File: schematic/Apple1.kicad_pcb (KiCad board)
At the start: 2 copper layers, 167.5 x 124.7 mm, 65 parts, among them J1 RCJ-041, J2 USB_A, J4 PWR, J5 ARM_JTAG_SWD, J6 SLOT, J7 EDGE, J8 12V, J9 -12V, SW1 RST, SW2 CLEAR, SW3 PWR, U1 WD65C02, U10 L7805, U2 6821 (W65C21N), U3 ATSAMD21E18A-A, U4 74LS138, U5 AT28C64B-15PU, U6 AS6C62256, U7 74HC00, U9 LD33CV

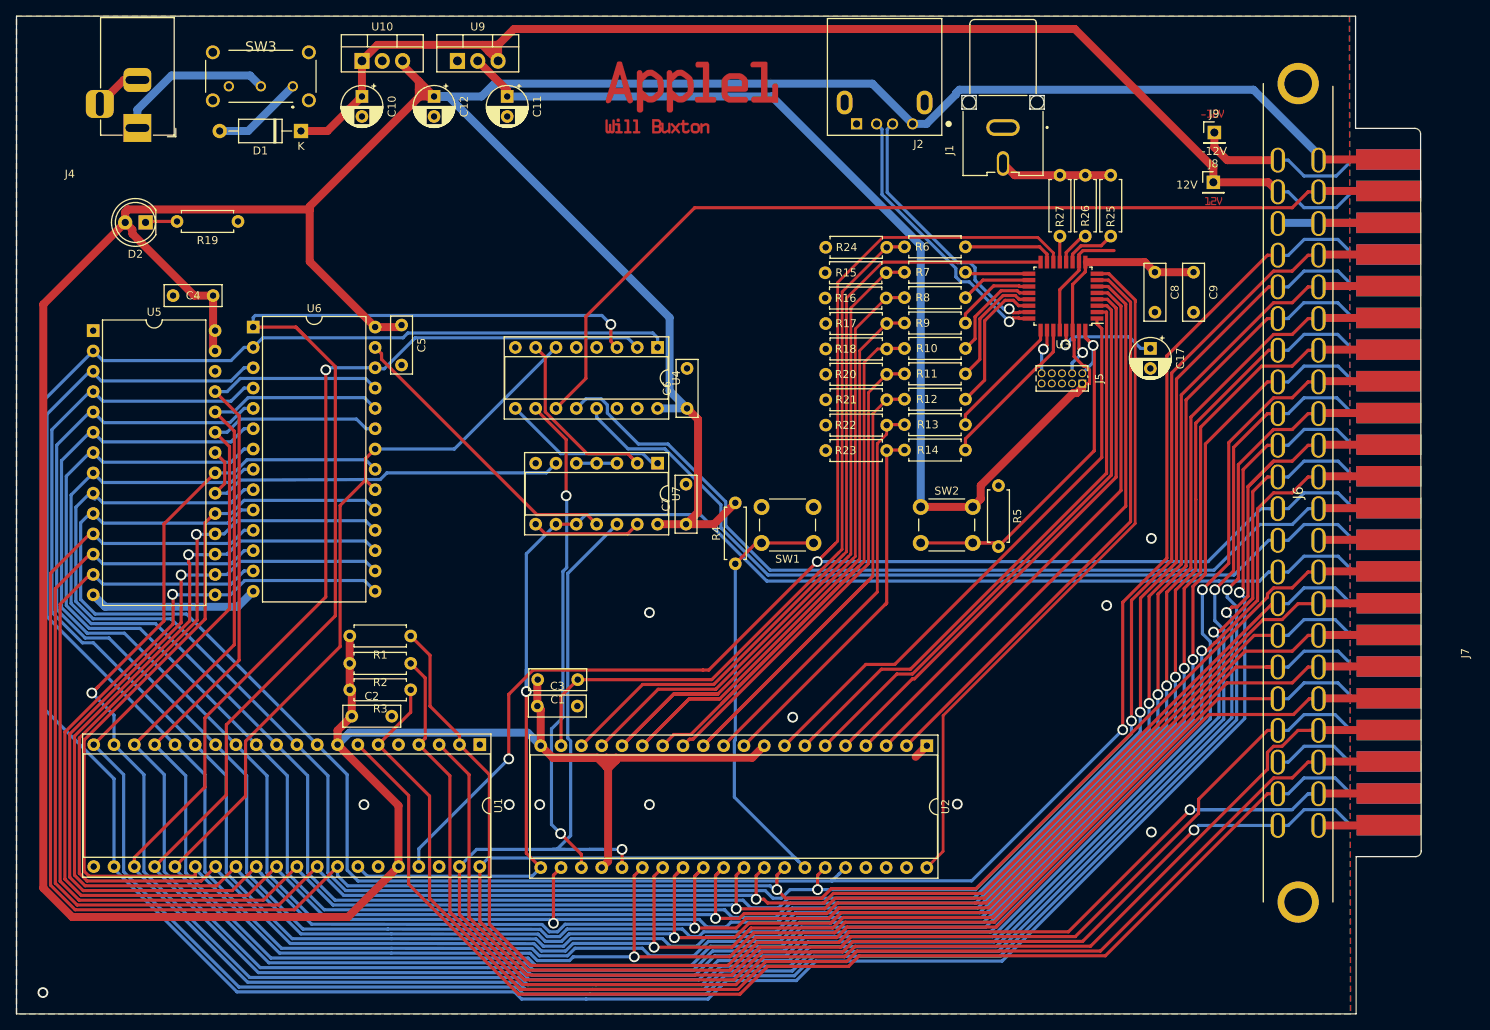
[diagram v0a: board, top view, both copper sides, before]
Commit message: updated pcb with electroplater
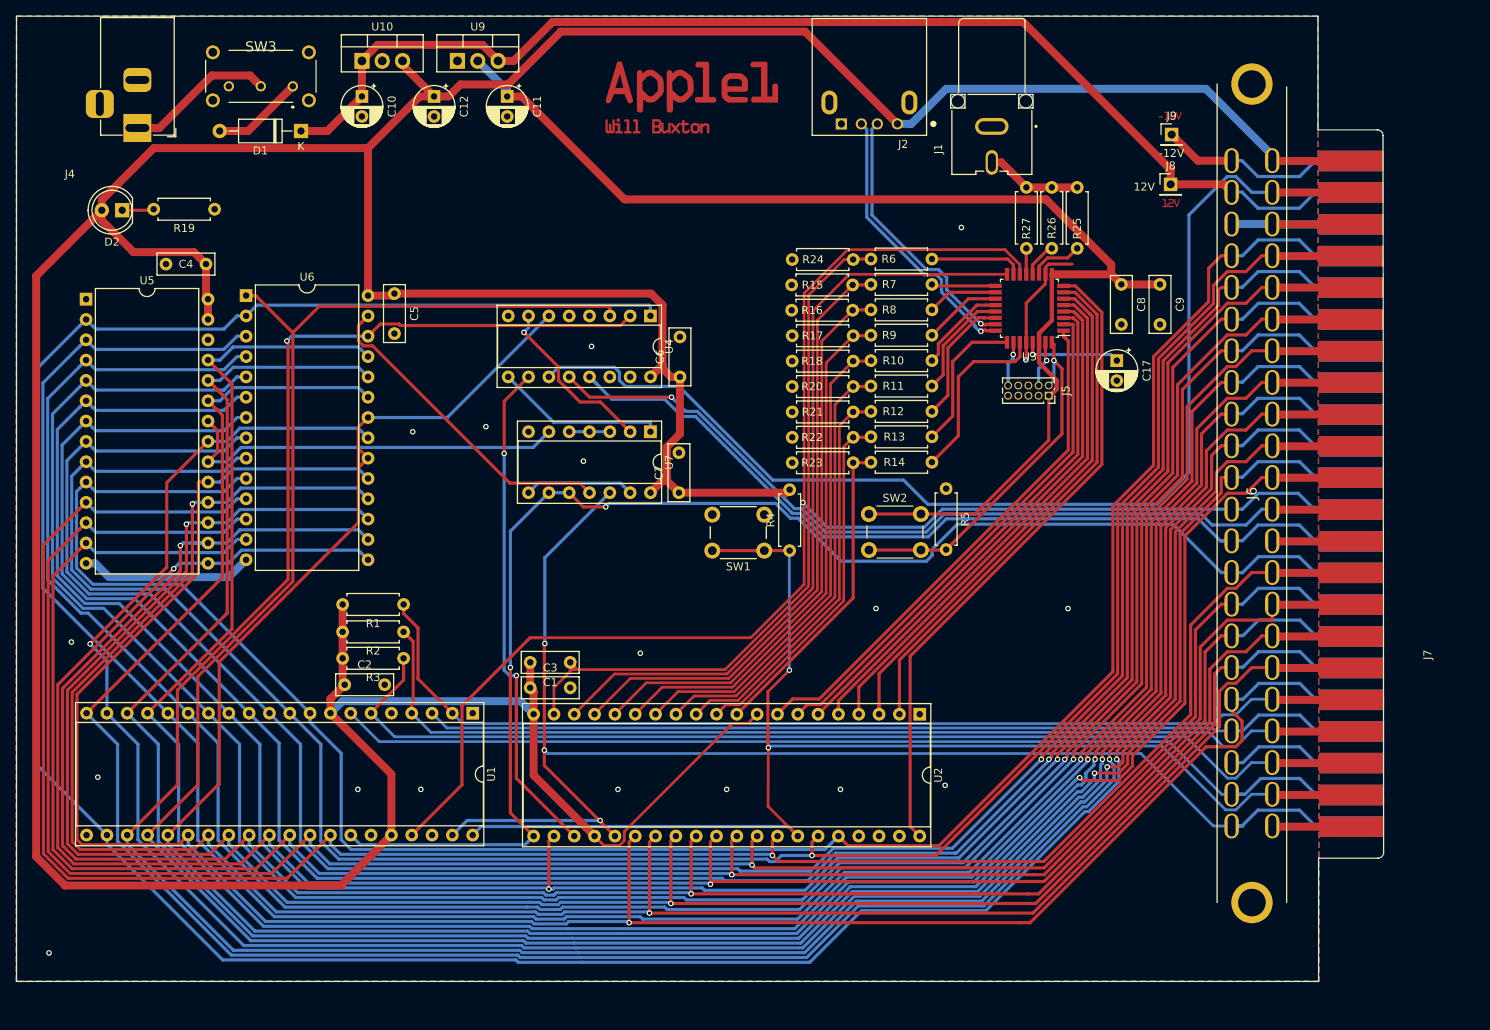
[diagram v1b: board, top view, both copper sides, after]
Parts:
- moved R4 6.99 mm to (128.4, 84.5)
- moved R5 6.55 mm to (148.0, 76.7)
- moved SW2 6.54 mm to (138.3, 79.9)
- moved SW1 6.23 mm to (125.2, 84.5)
- moved J6 5.78 mm to (188.7, 118.9)
- moved G*** 5.34 mm to (176.5, 42.9)
- moved J8 5.34 mm to (176.0, 38.7)
- moved J9 5.34 mm to (176.1, 32.4)
- moved G*** 5.34 mm to (176.0, 32.0)
- moved J7 4.70 mm to (207.6, 97.5)
- moved J5 4.46 mm to (160.8, 65.1)
- moved C17 4.46 mm to (169.3, 60.7)
- moved C8 4.46 mm to (169.9, 51.2)
- moved C9 4.46 mm to (174.7, 51.2)
- moved R10 4.46 mm to (146.2, 60.7)
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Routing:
- net /RESET: track 238.1 -> 166.8 mm, vias 1 -> 2
- net /PHI1O: track 156.4 -> 117.4 mm
- net /IQR: track 170.5 -> 131.9 mm
- net /RDY: track 168.5 -> 130.3 mm
- net /PB2: track 84.2 -> 50.2 mm
- net /NMI: track 166.9 -> 136.4 mm
- net /PHI2O: track 207.0 -> 177.1 mm, vias 2 -> 3
- net /PB4: track 89.6 -> 60.7 mm
- net /SYNC: track 161.1 -> 132.3 mm
- net /$C000: track 119.9 -> 145.1 mm
- net /A14: track 338.6 -> 316.7 mm, vias 2 -> 1
- net /PB6: track 89.8 -> 71.3 mm
- net /PB5: track 82.0 -> 66.0 mm
- net VCC: track 567.8 -> 553.1 mm
- net /A10: track 295.0 -> 284.0 mm
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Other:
- board size 167.5 x 124.7 mm -> 162.8 x 120.7 mm
- net class Default: via_dia 1.35 -> 0.7; via_drill 0.9 -> 0.4
- net class Thic: via_dia 1.35 -> 1; via_drill 0.9 -> 0.6

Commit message: rpi final
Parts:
- removed G***: LOGO, Apple1Title:n12v
- removed G***: LOGO, Apple1Title:12v
- removed G***: LOGO, Title:title
- added C13: 47uF, Capacitor_SMD:C_1206_3216Metric, F.Cu at (158.8, 74.6)
- added C14: 47uF, Capacitor_SMD:C_1206_3216Metric, F.Cu at (178.5, 62.6)
- added C15: 47uF, Capacitor_SMD:C_1206_3216Metric, F.Cu at (164.4, 74.6)
- added C16: 4.7uF, Capacitor_SMD:C_0603_1608Metric_Pad1.08x0.95mm_HandSolder, F.Cu at (172.2, 73.6)
- added C18: 0.1uF, Capacitor_SMD:C_0603_1608Metric_Pad1.08x0.95mm_HandSolder, F.Cu at (195.5, 76.7)
- added C19: 10uF, Capacitor_SMD:C_0603_1608Metric_Pad1.08x0.95mm_HandSolder, F.Cu at (117.5, 64.5)
- added C20: 10uF, Capacitor_SMD:C_0603_1608Metric_Pad1.08x0.95mm_HandSolder, F.Cu at (113.1, 64.5)
- added C21: 0.47uF, Capacitor_SMD:C_0603_1608Metric_Pad1.08x0.95mm_HandSolder, F.Cu at (108.8, 64.5)
- added C22: 0.47uF, Capacitor_SMD:C_0603_1608Metric_Pad1.08x0.95mm_HandSolder, F.Cu at (145.4, 62.9)
- added J3: SLOT, 307-044-520-202:307044520202, F.Cu at (244.5, 128.4)
- added L1: 4.7uH, Inductor_SMD:L_Bourns-SRN4018, F.Cu at (141.6, 61.9)
- added L2: 4.7uH, Inductor_SMD:L_Bourns-SRN4018, F.Cu at (135.5, 61.9)
- added Q1: DMG1012T, Package_TO_SOT_SMD:SOT-523, F.Cu at (171.7, 76.4)
- added Q2: DMG1012T, Package_TO_SOT_SMD:SOT-523, F.Cu at (210.2, 68.4)
- added R28: 2k, Resistor_SMD:R_0603_1608Metric_Pad0.98x0.95mm_HandSolder, F.Cu at (191.2, 76.7)
- added R29: 100k, Resistor_SMD:R_0603_1608Metric, F.Cu at (206.1, 72.6)
- added U11: AP2331W, Package_TO_SOT_SMD:SOT-23, F.Cu at (206.4, 61.5)
- added U12: AP7315DQ-2.5, Package_TO_SOT_SMD:SOT-23-5, F.Cu at (135.6, 50.2)
- added U8: AT28C64B-15PU, Package_DIP:DIP-28_W15.24mm, F.Cu at (137.0, 116.6)
- C1: value 0.01uF -> 0.33uF; footprint Capacitor_THT:C_Rect_L7.0mm_W2.5mm_P5.00mm -> Capacitor_SMD:C_0603_1608Metric_Pad1.08x0.95mm_HandSolder
- C10: value 10uF -> 0.1uF; footprint Capacitor_THT:CP_Radial_D5.0mm_P2.50mm -> Capacitor_THT:C_Rect_L7.0mm_W2.5mm_P5.00mm
- C11: footprint Capacitor_THT:CP_Radial_D5.0mm_P2.50mm -> Capacitor_SMD:C_0603_1608Metric_Pad1.08x0.95mm_HandSolder
- C12: value 1uF -> 10uF; footprint Capacitor_THT:CP_Radial_D5.0mm_P2.50mm -> Capacitor_SMD:C_0603_1608Metric_Pad1.08x0.95mm_HandSolder
- C17: value 1uF -> 0.1uF; footprint Capacitor_THT:CP_Radial_D5.0mm_P2.50mm -> Capacitor_SMD:C_0603_1608Metric_Pad1.08x0.95mm_HandSolder
- C2, C3: footprint Capacitor_THT:C_Rect_L7.0mm_W2.5mm_P5.00mm -> Capacitor_SMD:C_0603_1608Metric_Pad1.08x0.95mm_HandSolder
- C4: value 0.1uF -> 0.01uF
- J1: value RCJ-041 -> PWR; footprint CUI_RCJ-041 -> Connector_BarrelJack:BarrelJack_CUI_PJ-102AH_Horizontal
- J2: value USB_A -> EDGE; footprint UJ2-AH-4-TH:CUI_UJ2-AH-4-TH -> Connector_PCBEdge:EDAC_Edge_307-044-520-202
- J4: value PWR -> 12V; footprint Connector_BarrelJack:BarrelJack_Horizontal -> Connector_PinHeader_2.54mm:PinHeader_1x01_P2.54mm_Vertical
- J5: value ARM_JTAG_SWD -> -12V; footprint Connector_PinSocket_1.27mm:PinSocket_2x05_P1.27mm_Vertical -> Connector_PinHeader_2.54mm:PinHeader_1x01_P2.54mm_Vertical
- J6: value SLOT -> USB_A; footprint 307-044-520-202:307044520202 -> UJ2-AH-4-TH:CUI_UJ2-AH-4-TH
- J7: value EDGE -> RCJ-041; footprint Connector_PCBEdge:EDAC_Edge_307-044-520-202 -> CUI_RCJ-041
- J8: value 12V -> Micro_SD_Card_Det; footprint Connector_PinHeader_2.54mm:PinHeader_1x01_P2.54mm_Vertical -> Connector_Card:microSD_HC_Molex_104031-0811
- J9: value -12V -> HDMI_A; footprint Connector_PinHeader_2.54mm:PinHeader_1x01_P2.54mm_Vertical -> 10029449-111RLF:10029449111RLF
- R10, R11, R12, R13, R14, R6, R7, R8, R9: value 1K -> 2k; footprint Resistor_THT:R_Axial_DIN0207_L6.3mm_D2.5mm_P7.62mm_Horizontal -> Resistor_SMD:R_0603_1608Metric_Pad0.98x0.95mm_HandSolder
- R15, R16, R17, R18, R20, R21, R22, R23, R24: value 2k -> 1K; footprint Resistor_THT:R_Axial_DIN0207_L6.3mm_D2.5mm_P7.62mm_Horizontal -> Resistor_SMD:R_0603_1608Metric_Pad0.98x0.95mm_HandSolder
- R19: value 330 -> 100k; footprint Resistor_THT:R_Axial_DIN0207_L6.3mm_D2.5mm_P7.62mm_Horizontal -> Resistor_SMD:R_0603_1608Metric
- R25: footprint Resistor_THT:R_Axial_DIN0207_L6.3mm_D2.5mm_P7.62mm_Horizontal -> Resistor_SMD:R_0603_1608Metric_Pad0.98x0.95mm_HandSolder
- R26: value 560 -> 100k; footprint Resistor_THT:R_Axial_DIN0207_L6.3mm_D2.5mm_P7.62mm_Horizontal -> Resistor_SMD:R_0603_1608Metric_Pad0.98x0.95mm_HandSolder
- R27: value 220 -> 100k; footprint Resistor_THT:R_Axial_DIN0207_L6.3mm_D2.5mm_P7.62mm_Horizontal -> Resistor_SMD:R_0603_1608Metric_Pad0.98x0.95mm_HandSolder
- R5: value 3.3K -> 330
- SW1: value RST -> PWR; footprint Button_Switch_THT:SW_PUSH_6mm -> EG1224:EG1224
- SW2: value CLEAR -> RST
- SW3: value PWR -> CLEAR; footprint EG1224:EG1224 -> Button_Switch_THT:SW_PUSH_6mm
- U1: value WD65C02 -> 74LS138; footprint Package_DIP:DIP-40_W15.24mm_Socket -> Package_DIP:DIP-16_W7.62mm_Socket
- U10: value L7805 -> ESD5384; footprint Package_TO_SOT_THT:TO-220-3_Vertical -> SW-On-Semi:WLCSP9-1.14x1.14mm
- U2: value 6821 (W65C21N) -> AS6C62256; footprint Package_DIP:DIP-40_W15.24mm_Socket -> Package_DIP:DIP-28_W15.24mm
- U3: value ATSAMD21E18A-A -> WD65C02; footprint Package_QFP:TQFP-32_7x7mm_P0.8mm -> Package_DIP:DIP-40_W15.24mm_Socket
- U4: value 74LS138 -> 74HC00; footprint Package_DIP:DIP-16_W7.62mm_Socket -> Package_DIP:DIP-14_W7.62mm_Socket
- U5: value AT28C64B-15PU -> PAM2306AYPKE; footprint Package_DIP:DIP-28_W15.24mm -> Package_DFN_QFN:WDFN-12-1EP_3x3mm_P0.45mm_EP1.7x2.5mm
- U6: value AS6C62256 -> 6821 (W65C21N); footprint Package_DIP:DIP-28_W15.24mm -> Package_DIP:DIP-40_W15.24mm_Socket
- U7: value 74HC00 -> L7805; footprint Package_DIP:DIP-14_W7.62mm_Socket -> Package_TO_SOT_THT:TO-220-3_Vertical
- U9: value LD33CV -> RaspberryPi-CM3+L; footprint Package_TO_SOT_THT:TO-220-3_Vertical -> 1717254-4:17172544
- moved SW3 151.3 mm to (207.3, 81.4), turned to 0 degrees
- moved J2 143.0 mm to (263.1, 106.9), turned to 90 degrees
- moved U6 131.9 mm to (175.9, 116.5), turned to 90 degrees
- moved U10 112.7 mm to (177.1, 70.7)
- moved U5 107.1 mm to (147.3, 61.4)
- moved U9 106.7 mm to (189.9, 51.1)
- moved R19 95.4 mm to (149.6, 62.9), turned to 0 degrees
- moved D2 94.5 mm to (125.1, 91.9), turned to 0 degrees
- moved J4 94.2 mm to (136.3, 61.4), turned to 0 degrees
- moved C2 87.2 mm to (149.8, 60.3)
- moved U3 85.7 mm to (175.8, 138.0), turned to 90 degrees
- moved R15 82.6 mm to (210.8, 60.5)
- moved SW2 80.8 mm to (219.1, 81.0)
- moved C10 80.1 mm to (143.3, 69.4), turned to 0 degrees
- moved J6 80.1 mm to (166.2, 42.0), turned to 180 degrees
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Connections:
- C1 pad 1: /CB2 -> +12V
- C1 pad 2: VCC -> GND
- C10 pad 1: +12V -> +5V
- C11 pad 1: +3V3 -> +5V
- C12 pad 1: VCC -> +5V
- C17 pad 1: Net-(C17-Pad1) -> +5V
- C2 pad 1: VCC -> GND
- C2 pad 2: GND -> Net-(C2-Pad2)
- C3 pad 1: VCC -> +5V
- C4 pad 1: VCC -> /CB2
- C4 pad 2: GND -> +5V
- C5 pad 1: VCC -> +5V
- C6 pad 1: VCC -> +5V
- C7 pad 1: VCC -> +5V
- C8 pad 1: +3V3 -> +5V
- C9 pad 1: +3V3 -> +5V
- D2 pad 2: VCC -> +5V
- J1 pad 1: GND -> Net-(J1-Pad1)
- J1 pad 2: Net-(J1-Pad2) -> GND
- J2 pad 1: VCC -> /RF
- J2 pad 2: /KEYD- -> /PHI2O
- J2 pad 3: /KEYD+ -> /RESET
- J2 pad 4: GND -> /SYNC
- J2 pad 5: GND -> /NMI
- J4 pad 1: Net-(J4-Pad1) -> +12V
- J5 pad 1: +3V3 -> -12V
- J6 pad 1: /RF -> +5V
- J6 pad 2: /PHI2O -> /RaspberryPi/USB_D-
- J6 pad 3: /RESET -> /RaspberryPi/USB_D+
- J6 pad 4: /SYNC -> GND
- J6 pad 5: /NMI -> GND
- J7 pad 1: /RF -> GND
- J7 pad 2: /PHI2O -> /RaspberryPi/TVDAC
- J8 pad 1: +12V -> /RaspberryPi/SDX_D2
- J9 pad 1: -12V -> /RaspberryPi/HDMI_D2_P
- R1 pad 2: VCC -> +5V
- R10 pad 1: Net-(R10-Pad1) -> GND
- R11 pad 1: Net-(R11-Pad1) -> GND
- R11 pad 2: /PB3 -> /PB5
- R12 pad 1: Net-(R12-Pad1) -> GND
- R12 pad 2: /PB2 -> /PB6
- R13 pad 1: Net-(R13-Pad1) -> GND
- R13 pad 2: /PB1 -> /DA
- R14 pad 1: Net-(R14-Pad1) -> GND
- R14 pad 2: /PB0 -> /CB2
- R15 pad 1: GND -> Net-(R15-Pad1)
- R15 pad 2: /DA -> /RESET
- R16 pad 1: GND -> Net-(R16-Pad1)
- R16 pad 2: /PB6 -> /PB0
- R17 pad 1: GND -> Net-(R17-Pad1)
- R17 pad 2: /PB5 -> /PB1
- R18 pad 1: GND -> Net-(R18-Pad1)
- R18 pad 2: /PB4 -> /PB2
- R19 pad 1: GND -> +5V
- R19 pad 2: Net-(D2-Pad1) -> Net-(C2-Pad2)
- R2 pad 2: VCC -> +5V
- R20 pad 1: GND -> Net-(R20-Pad1)
- R21 pad 1: GND -> Net-(R21-Pad1)
- R21 pad 2: /PB2 -> /PB4
- R22 pad 1: GND -> Net-(R22-Pad1)
- R22 pad 2: /PB1 -> /PB5
- R23 pad 1: GND -> Net-(R23-Pad1)
- R23 pad 2: /PB0 -> /PB6
- R24 pad 1: GND -> Net-(R24-Pad1)
- R24 pad 2: /CB2 -> /DA
- R25 pad 2: Net-(J1-Pad2) -> /CB2
- R26 pad 1: Net-(R26-Pad1) -> /STROBE
- R26 pad 2: Net-(J1-Pad2) -> GND
- R27 pad 1: Net-(R27-Pad1) -> /PA0
- R27 pad 2: Net-(J1-Pad2) -> GND
- R3 pad 2: VCC -> +5V
- R4 pad 2: VCC -> +5V
- R5 pad 2: /SWDIO -> Net-(D2-Pad1)
- R6 pad 1: Net-(R6-Pad1) -> GND
- R6 pad 2: /CB2 -> /PB0
- R7 pad 1: Net-(R7-Pad1) -> GND
- R7 pad 2: /DA -> /PB1
- R8 pad 1: Net-(R8-Pad1) -> GND
- R8 pad 2: /PB6 -> /PB2
- R9 pad 1: Net-(R9-Pad1) -> GND
- R9 pad 2: /PB5 -> /PB3
- SW1 pad 1: /RESET -> Net-(D1-Pad2)
- SW1 pad 2: GND -> Net-(J1-Pad1)
- SW2 pad 1: +3V3 -> /RESET
- SW2 pad 2: /SWDIO -> GND
- SW3 pad 1: Net-(D1-Pad2) -> GND
- SW3 pad 2: Net-(J4-Pad1) -> /RaspberryPi/CLEAR
- U1 pad 1: (no net) -> /A12
- U1 pad 10: /A1 -> /$D000
- U1 pad 11: /A2 -> /$C000
- U1 pad 12: /A3 -> /$B000
- U1 pad 13: /A4 -> /$A000
- U1 pad 14: /A5 -> (no net)
- U1 pad 15: /A6 -> (no net)
- U1 pad 16: /A7 -> +5V
- U1 pad 2: /RDY -> /A13
- U1 pad 3: /PHI1O -> /A14
- U1 pad 4: /IQR -> GND
- U1 pad 5: (no net) -> GND
- U1 pad 6: /NMI -> /A15
- U1 pad 7: /SYNC -> /$F000
- U1 pad 8: VCC -> GND
- U1 pad 9: /A0 -> /$E000
- U2 pad 1: GND -> /A14
- U2 pad 10: /PB0 -> /A0
- U2 pad 11: /PB1 -> /D0
- U2 pad 12: /PB2 -> /D1
- U2 pad 13: /PB3 -> /D2
- U2 pad 14: /PB4 -> GND
- U2 pad 15: /PB5 -> /D3
- U2 pad 16: /PB6 -> /D4
- U2 pad 17: /DA -> /D5
- U2 pad 18: /RDA -> /D6
- U2 pad 19: /CB2 -> /D7
- U2 pad 2: /PA0 -> /A12
- U2 pad 20: VCC -> /A15
- U2 pad 21: /RW -> /A10
- U2 pad 22: /A4 -> /A15
- U2 pad 23: /$D000 -> /A11
- U2 pad 24: VCC -> /A9
- U2 pad 25: /PHI2O -> /A8
- U2 pad 26: /D7 -> /A13
- U2 pad 27: /D6 -> /WE
- U2 pad 28: /D5 -> +5V
- U2 pad 3: /PA1 -> /A7
- U2 pad 4: /PA2 -> /A6
- U2 pad 5: /PA3 -> /A5
- U2 pad 6: /PA4 -> /A4
- U2 pad 7: /PA5 -> /A3
- U2 pad 8: /PA6 -> /A2
- U2 pad 9: VCC -> /A1
- U3 pad 1: /PA6 -> (no net)
- U3 pad 10: GND -> /A1
- U3 pad 11: Net-(R25-Pad1) -> /A2
- U3 pad 12: Net-(R26-Pad1) -> /A3
- U3 pad 13: Net-(R27-Pad1) -> /A4
- U3 pad 14: /PHI2 -> /A5
- U3 pad 15: Net-(R6-Pad1) -> /A6
- U3 pad 16: /RDA -> /A7
- U3 pad 17: Net-(R7-Pad1) -> /A8
- U3 pad 18: Net-(R8-Pad1) -> /A9
- U3 pad 19: Net-(R9-Pad1) -> /A10
- U3 pad 2: /PA5 -> /RDY
- U3 pad 20: Net-(R10-Pad1) -> /A11
- U3 pad 21: Net-(R11-Pad1) -> GND
- U3 pad 22: Net-(R12-Pad1) -> /A12
- U3 pad 23: /KEYD- -> /A13
- U3 pad 24: /KEYD+ -> /A14
- U3 pad 25: Net-(R13-Pad1) -> /A15
- U3 pad 26: /RST -> /D7
- U3 pad 27: Net-(R14-Pad1) -> /D6
- U3 pad 28: GND -> /D5
- U3 pad 29: Net-(C17-Pad1) -> /D4
- U3 pad 3: /PA4 -> /PHI1O
- U3 pad 30: +3V3 -> /D3
- U3 pad 31: /SWCLK -> /D2
- U3 pad 32: /SWDIO -> /D1
- U3 pad 4: /PA3 -> /IQR
- U3 pad 5: /PA2 -> (no net)
- U3 pad 6: /PA1 -> /NMI
- U3 pad 7: /PA0 -> /SYNC
- U3 pad 8: /STROBE -> +5V
- U3 pad 9: +3V3 -> /A0
- U4 pad 1: /A12 -> /$E000
- U4 pad 10: /$D000 -> /RW
- U4 pad 11: /$C000 -> /WE
- U4 pad 12: /$B000 -> /PHI2O
- U4 pad 13: /$A000 -> Net-(U4-Pad13)
- U4 pad 14: (no net) -> +5V
- U4 pad 2: /A13 -> /$F000
- U4 pad 3: /A14 -> Net-(U4-Pad3)
- U4 pad 4: GND -> Net-(U4-Pad3)
- U4 pad 5: GND -> Net-(U4-Pad3)
- U4 pad 6: /A15 -> Net-(U4-Pad6)
- U4 pad 7: /$F000 -> GND
- U4 pad 8: GND -> Net-(U4-Pad13)
- U4 pad 9: /$E000 -> /RW
- U5 pad 1: (no net) -> +5V
- U5 pad 10: /A0 -> +1V8
- U5 pad 11: /D0 -> (no net)
- U5 pad 12: /D1 -> Net-(C2-Pad2)
- U5 pad 13: /D2 -> GND
- U5 pad 2: /A12 -> Net-(L2-Pad1)
- U5 pad 3: /A7 -> GND
- U5 pad 4: /A6 -> +3V3
- U5 pad 5: /A5 -> (no net)
- U5 pad 6: /A4 -> +5V
- U5 pad 7: /A3 -> +5V
- U5 pad 8: /A2 -> Net-(L1-Pad1)
- U5 pad 9: /A1 -> GND
- U6 pad 1: /A14 -> GND
- U6 pad 10: /A0 -> /PB0
- U6 pad 11: /D0 -> /PB1
- U6 pad 12: /D1 -> /PB2
- U6 pad 13: /D2 -> /PB3
- U6 pad 14: GND -> /PB4
- U6 pad 15: /D3 -> /PB5
- U6 pad 16: /D4 -> /PB6
- U6 pad 17: /D5 -> /DA
- U6 pad 18: /D6 -> /RDA
- U6 pad 19: /D7 -> /CB2
- U6 pad 2: /A12 -> /PA0
- U6 pad 20: /A15 -> +5V
- U6 pad 21: /A10 -> /RW
- U6 pad 22: /A15 -> /A4
- U6 pad 23: /A11 -> /$D000
- U6 pad 24: /A9 -> +5V
- U6 pad 25: /A8 -> /PHI2O
- U6 pad 26: /A13 -> /D7
- U6 pad 27: /WE -> /D6
- U6 pad 28: VCC -> /D5
- U6 pad 3: /A7 -> /PA1
- U6 pad 4: /A6 -> /PA2
- U6 pad 5: /A5 -> /PA3
- U6 pad 6: /A4 -> /PA4
- U6 pad 7: /A3 -> /PA5
- U6 pad 8: /A2 -> /PA6
- U6 pad 9: /A1 -> +5V
- U7 pad 1: /$E000 -> +12V
- U7 pad 2: /$F000 -> GND
- U7 pad 3: Net-(U7-Pad3) -> +5V
- U9 pad 2: +3V3 -> (no net)
- U9 pad 3: +12V -> Net-(R15-Pad1)
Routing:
- net VCC: track 553.1 -> 0.00 mm
- net /A12: track 352.5 -> 0.00 mm, vias 1 -> 0
- net /A14: track 316.7 -> 0.00 mm, vias 1 -> 0
- net /A13: track 315.8 -> 0.00 mm, vias 2 -> 0
- net /A11: track 292.3 -> 0.00 mm, vias 1 -> 0
- net /A7: track 290.1 -> 0.00 mm, vias 1 -> 0
- net /A9: track 289.3 -> 0.00 mm, vias 1 -> 0
- net /A4: track 288.2 -> 0.00 mm, vias 2 -> 0
- net /A8: track 287.7 -> 0.00 mm, vias 1 -> 0
- net /A6: track 287.7 -> 0.00 mm, vias 1 -> 0
- net /A15: track 287.2 -> 0.00 mm, vias 1 -> 0
- net /A10: track 284.0 -> 0.00 mm, vias 2 -> 0
- net /A5: track 283.3 -> 0.00 mm, vias 1 -> 0
- net /A3: track 276.8 -> 0.00 mm, vias 1 -> 0
- net /A2: track 274.9 -> 0.00 mm, vias 1 -> 0
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- removed copper zone on B.Cu, net GND
- removed copper zone on F.Cu, net GND
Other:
- board size 162.8 x 120.7 mm -> 8.2 x 91 mm
- copper layers 2 -> 4
- net class HDMI_dPair added: clearance 0.2, trace_width 0.2, via_dia 0.5, via_drill 0.2
- net class PWR added: clearance 0.2, trace_width 1, via_dia 1, via_drill 0.6
- net class Thic removed
- net class USB_dPair added: clearance 0.2, trace_width 0.2, via_dia 1, via_drill 0.6
- rule trace_min: 0.2 -> 0.1
- rule via_min_drill: 0.3 -> 0.127
- rule via_min_size: 0.4 -> 0.3

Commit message: completed schematic
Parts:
- removed R12, R13, R14, R28: 2k, Resistor_SMD:R_0603_1608Metric_Pad0.98x0.95mm_HandSolder
- removed R15, R16, R17, R18, R20, R21, R22, R23, R24, R25: 1K, Resistor_SMD:R_0603_1608Metric_Pad0.98x0.95mm_HandSolder
- removed R19, R29: 100k, Resistor_SMD:R_0603_1608Metric
- removed R26, R27: 100k, Resistor_SMD:R_0603_1608Metric_Pad0.98x0.95mm_HandSolder
- added U13: TXB0104D, Package_SO:SOIC-14_3.9x8.7mm_P1.27mm, F.Cu at (193.0, 68.7)
- added U14: TXB0104D, Package_SO:SOIC-14_3.9x8.7mm_P1.27mm, F.Cu at (224.7, 68.7)
- added U15: TXB0104D, Package_SO:SOIC-14_3.9x8.7mm_P1.27mm, F.Cu at (203.6, 68.7)
- added U16: ESD5384, SW-On-Semi:WLCSP9-1.14x1.14mm, F.Cu at (201.5, 34.0)
- added U17: AP2331W, Package_TO_SOT_SMD:SOT-23, F.Cu at (208.5, 34.5)
- C10: value 0.1uF -> 0.01uF
- C11, C12: value 10uF -> 0.1uF; footprint Capacitor_SMD:C_0603_1608Metric_Pad1.08x0.95mm_HandSolder -> Capacitor_THT:C_Rect_L7.0mm_W2.5mm_P5.00mm
- C13, C14, C15: value 47uF -> 0.1uF; footprint Capacitor_SMD:C_1206_3216Metric -> Capacitor_THT:C_Rect_L7.0mm_W2.5mm_P5.00mm
- C16: value 4.7uF -> 0.1uF; footprint Capacitor_SMD:C_0603_1608Metric_Pad1.08x0.95mm_HandSolder -> Capacitor_THT:C_Rect_L7.0mm_W2.5mm_P5.00mm
- C17, C18: value 0.1uF -> 47uF; footprint Capacitor_SMD:C_0603_1608Metric_Pad1.08x0.95mm_HandSolder -> Capacitor_SMD:C_1206_3216Metric
- C19: value 10uF -> 47uF; footprint Capacitor_SMD:C_0603_1608Metric_Pad1.08x0.95mm_HandSolder -> Capacitor_SMD:C_1206_3216Metric
- C20: value 10uF -> 4.7uF
- C21, C22: value 0.47uF -> 0.1uF
- C4: value 0.01uF -> 10uF; footprint Capacitor_THT:C_Rect_L7.0mm_W2.5mm_P5.00mm -> Capacitor_SMD:C_0603_1608Metric_Pad1.08x0.95mm_HandSolder
- C5, C6, C7: value 0.1uF -> 10uF; footprint Capacitor_THT:C_Rect_L7.0mm_W2.5mm_P5.00mm -> Capacitor_SMD:C_0603_1608Metric_Pad1.08x0.95mm_HandSolder
- C8, C9: value 0.1uF -> 0.47uF; footprint Capacitor_THT:C_Rect_L7.0mm_W2.5mm_P5.00mm -> Capacitor_SMD:C_0603_1608Metric_Pad1.08x0.95mm_HandSolder
- J6: value USB_A -> Micro_SD_Card_Det; footprint UJ2-AH-4-TH:CUI_UJ2-AH-4-TH -> Connector_Card:microSD_HC_Molex_104031-0811
- J8: value Micro_SD_Card_Det -> USB_A; footprint Connector_Card:microSD_HC_Molex_104031-0811 -> UJ2-AH-4-TH:CUI_UJ2-AH-4-TH
- R10, R11, R7, R8, R9: value 2k -> 100k; footprint Resistor_SMD:R_0603_1608Metric_Pad0.98x0.95mm_HandSolder -> Resistor_SMD:R_0603_1608Metric
- R4: value 3.3k -> 100k; footprint Resistor_THT:R_Axial_DIN0207_L6.3mm_D2.5mm_P7.62mm_Horizontal -> Resistor_SMD:R_0603_1608Metric
- R5: value 330 -> 3.3k
- R6: value 2k -> 330; footprint Resistor_SMD:R_0603_1608Metric_Pad0.98x0.95mm_HandSolder -> Resistor_THT:R_Axial_DIN0207_L6.3mm_D2.5mm_P7.62mm_Horizontal
- U1: value 74LS138 -> WD65C02; footprint Package_DIP:DIP-16_W7.62mm_Socket -> Package_DIP:DIP-40_W15.24mm_Socket
- U10: value ESD5384 -> AP7315DQ-2.5; footprint SW-On-Semi:WLCSP9-1.14x1.14mm -> Package_TO_SOT_SMD:SOT-23-5
- U11: value AP2331W -> TXB0104D; footprint Package_TO_SOT_SMD:SOT-23 -> Package_SO:SOIC-14_3.9x8.7mm_P1.27mm
- U12: value AP7315DQ-2.5 -> TXB0104D; footprint Package_TO_SOT_SMD:SOT-23-5 -> Package_SO:SOIC-14_3.9x8.7mm_P1.27mm
- U2: value AS6C62256 -> 6821 (W65C21N); footprint Package_DIP:DIP-28_W15.24mm -> Package_DIP:DIP-40_W15.24mm_Socket
- U3: value WD65C02 -> AS6C62256; footprint Package_DIP:DIP-40_W15.24mm_Socket -> Package_DIP:DIP-28_W15.24mm
- U4: value 74HC00 -> AT28C64B-15PU; footprint Package_DIP:DIP-14_W7.62mm_Socket -> Package_DIP:DIP-28_W15.24mm
- U5: value PAM2306AYPKE -> 74LS138; footprint Package_DFN_QFN:WDFN-12-1EP_3x3mm_P0.45mm_EP1.7x2.5mm -> Package_DIP:DIP-16_W7.62mm_Socket
- U6: value 6821 (W65C21N) -> RaspberryPi-CM3+L; footprint Package_DIP:DIP-40_W15.24mm_Socket -> 1717254-4:17172544
- U8: value AT28C64B-15PU -> PAM2306AYPKE; footprint Package_DIP:DIP-28_W15.24mm -> Package_DFN_QFN:WDFN-12-1EP_3x3mm_P0.45mm_EP1.7x2.5mm
- U9: value RaspberryPi-CM3+L -> 74HC00; footprint 1717254-4:17172544 -> Package_DIP:DIP-14_W7.62mm_Socket
- moved C20 116.4 mm to (221.5, 22.2), turned to 270 degrees
- moved J4 112.1 mm to (244.5, 32.0)
- moved J5 112.1 mm to (249.1, 32.0)
- moved C21 106.7 mm to (211.2, 34.4), turned to 90 degrees
- moved U3 83.4 mm to (115.7, 80.1), turned to 0 degrees
- moved U12 80.8 mm to (214.2, 68.7), turned to 270 degrees
- moved U2 80.5 mm to (217.0, 128.4), turned to 270 degrees
- moved R1 79.0 mm to (161.4, 125.0), turned to 90 degrees
- moved U6 78.7 mm to (202.9, 42.5), turned to 0 degrees
- moved R2 73.0 mm to (156.3, 125.0), turned to 90 degrees
- moved R5 72.5 mm to (179.7, 69.0), turned to 270 degrees
- moved U8 71.1 mm to (153.2, 47.3), turned to 0 degrees
- moved R3 70.0 mm to (151.3, 125.0), turned to 90 degrees
- moved C22 66.9 mm to (205.9, 34.4), turned to 270 degrees
- moved J6 66.2 mm to (230.6, 26.6), turned to 270 degrees
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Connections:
- C10 pad 1: +5V -> /CB2
- C10 pad 2: GND -> +5V
- C13 pad 1: +1V8 -> +5V
- C14 pad 1: +3V3 -> +5V
- C16 pad 1: +3V3 -> +5V
- C17 pad 1: +5V -> +1V8
- C18 pad 1: +5VA -> +3V3
- C19 pad 1: +1V8 -> +5V
- C2 pad 1: GND -> +5V
- C2 pad 2: Net-(C2-Pad2) -> GND
- C21 pad 1: +3V3 -> +5V
- C22 pad 1: +2V5 -> +5VA
- C3 pad 1: +5V -> GND
- C3 pad 2: GND -> Net-(C3-Pad2)
- C4 pad 1: /CB2 -> +5V
- C4 pad 2: +5V -> GND
- C6 pad 1: +5V -> +1V8
- C7 pad 1: +5V -> +3V3
- C8 pad 1: +5V -> +3V3
- C9 pad 1: +5V -> +2V5
- J6 pad 1: +5V -> /RaspberryPi/SDX_D2
- J6 pad 2: /RaspberryPi/USB_D- -> /RaspberryPi/SDX_D3
- J6 pad 3: /RaspberryPi/USB_D+ -> /RaspberryPi/SDX_CMD
- J6 pad 4: GND -> +3V3
- J6 pad 5: GND -> /RaspberryPi/SDX_CLK
- J8 pad 1: /RaspberryPi/SDX_D2 -> +5V
- J8 pad 2: /RaspberryPi/SDX_D3 -> /RaspberryPi/USB_D-
- J8 pad 3: /RaspberryPi/SDX_CMD -> /RaspberryPi/USB_D+
- J8 pad 4: +3V3 -> GND
- J8 pad 5: /RaspberryPi/SDX_CLK -> GND
- R10 pad 1: GND -> /RaspberryPi/RP_DA
- R10 pad 2: /PB4 -> GND
- R11 pad 1: GND -> /RaspberryPi/HDMI_HPD_N
- R11 pad 2: /PB5 -> +1V8
- R4 pad 1: /RESET -> +5V
- R4 pad 2: +5V -> Net-(C3-Pad2)
- R5 pad 1: GND -> /RESET
- R5 pad 2: Net-(D2-Pad1) -> +5V
- R6 pad 2: /PB0 -> Net-(D2-Pad1)
- R7 pad 1: GND -> /RaspberryPi/RP_STB
- R7 pad 2: /PB1 -> GND
- R8 pad 1: GND -> /RaspberryPi/RP_PB6
- R8 pad 2: /PB2 -> GND
- R9 pad 1: GND -> /RaspberryPi/RP_PA0
- R9 pad 2: /PB3 -> GND
- U1 pad 1: /A12 -> (no net)
- U1 pad 10: /$D000 -> /A1
- U1 pad 11: /$C000 -> /A2
- U1 pad 12: /$B000 -> /A3
- U1 pad 13: /$A000 -> /A4
- U1 pad 14: (no net) -> /A5
- U1 pad 15: (no net) -> /A6
- U1 pad 16: +5V -> /A7
- U1 pad 2: /A13 -> /RDY
- U1 pad 3: /A14 -> /PHI1O
- U1 pad 4: GND -> /IQR
- U1 pad 5: GND -> (no net)
- U1 pad 6: /A15 -> /NMI
- U1 pad 7: /$F000 -> /SYNC
- U1 pad 8: GND -> +5V
- U1 pad 9: /$E000 -> /A0
- U11 pad 1: GND -> +3V3
- U11 pad 2: +5VA -> /RaspberryPi/RP_STB
- U11 pad 3: +5V -> /RaspberryPi/RP_PA0
- U12 pad 2: GND -> /RaspberryPi/RP_PB0
- U12 pad 3: +3V3 -> /RaspberryPi/RP_PB1
- U12 pad 4: (no net) -> /RaspberryPi/RP_PB2
- U12 pad 5: +2V5 -> /RaspberryPi/RP_PB3
- U2 pad 1: /A14 -> GND
- U2 pad 10: /A0 -> /PB0
- U2 pad 11: /D0 -> /PB1
- U2 pad 12: /D1 -> /PB2
- U2 pad 13: /D2 -> /PB3
- U2 pad 14: GND -> /PB4
- U2 pad 15: /D3 -> /PB5
- U2 pad 16: /D4 -> /PB6
- U2 pad 17: /D5 -> /DA
- U2 pad 18: /D6 -> /RDA
- U2 pad 19: /D7 -> /CB2
- U2 pad 2: /A12 -> /PA0
- U2 pad 20: /A15 -> +5V
- U2 pad 21: /A10 -> /RW
- U2 pad 22: /A15 -> /A4
- U2 pad 23: /A11 -> /$D000
- U2 pad 24: /A9 -> +5V
- U2 pad 25: /A8 -> /PHI2O
- U2 pad 26: /A13 -> /D7
- U2 pad 27: /WE -> /D6
- U2 pad 28: +5V -> /D5
- U2 pad 3: /A7 -> /PA1
- U2 pad 4: /A6 -> /PA2
- U2 pad 5: /A5 -> /PA3
- U2 pad 6: /A4 -> /PA4
- U2 pad 7: /A3 -> /PA5
- U2 pad 8: /A2 -> /PA6
- U2 pad 9: /A1 -> +5V
- U3 pad 1: (no net) -> /A14
- U3 pad 10: /A1 -> /A0
- U3 pad 11: /A2 -> /D0
- U3 pad 12: /A3 -> /D1
- U3 pad 13: /A4 -> /D2
- U3 pad 14: /A5 -> GND
- U3 pad 15: /A6 -> /D3
- U3 pad 16: /A7 -> /D4
- U3 pad 17: /A8 -> /D5
- U3 pad 18: /A9 -> /D6
- U3 pad 19: /A10 -> /D7
- U3 pad 2: /RDY -> /A12
- U3 pad 20: /A11 -> /A15
- U3 pad 21: GND -> /A10
- U3 pad 22: /A12 -> /A15
- U3 pad 23: /A13 -> /A11
- U3 pad 24: /A14 -> /A9
- U3 pad 25: /A15 -> /A8
- U3 pad 26: /D7 -> /A13
- U3 pad 27: /D6 -> /WE
- U3 pad 28: /D5 -> +5V
- U3 pad 3: /PHI1O -> /A7
- U3 pad 4: /IQR -> /A6
- U3 pad 5: (no net) -> /A5
- U3 pad 6: /NMI -> /A4
- U3 pad 7: /SYNC -> /A3
- U3 pad 8: +5V -> /A2
- U3 pad 9: /A0 -> /A1
- U4 pad 1: /$E000 -> (no net)
- U4 pad 10: /RW -> /A0
- U4 pad 11: /WE -> /D0
- U4 pad 12: /PHI2O -> /D1
- U4 pad 13: Net-(U4-Pad13) -> /D2
- U4 pad 14: +5V -> GND
- U4 pad 2: /$F000 -> /A12
- U4 pad 3: Net-(U4-Pad3) -> /A7
- U4 pad 4: Net-(U4-Pad3) -> /A6
- U4 pad 5: Net-(U4-Pad3) -> /A5
- U4 pad 6: Net-(U4-Pad6) -> /A4
- U4 pad 7: GND -> /A3
- U4 pad 8: Net-(U4-Pad13) -> /A2
- U4 pad 9: /RW -> /A1
- U5 pad 1: +5V -> /A12
- U5 pad 10: +1V8 -> /$D000
- U5 pad 11: (no net) -> /$C000
- U5 pad 12: Net-(C2-Pad2) -> /$B000
- U5 pad 13: GND -> /$A000
- U5 pad 2: Net-(L2-Pad1) -> /A13
- U5 pad 3: GND -> /A14
- U5 pad 4: +3V3 -> GND
- U5 pad 5: (no net) -> GND
- U5 pad 6: +5V -> /A15
- U5 pad 7: +5V -> /$F000
- U5 pad 8: Net-(L1-Pad1) -> GND
- U5 pad 9: GND -> /$E000
- U6 pad 10: /PB0 -> /RaspberryPi/SDX_CLK
- U6 pad 11: /PB1 -> (no net)
- U6 pad 12: /PB2 -> /RaspberryPi/SDX_CMD
- U6 pad 13: /PB3 -> GND
- U6 pad 14: /PB4 -> GND
- U6 pad 15: /PB5 -> (no net)
- U6 pad 16: /PB6 -> /RaspberryPi/SDX_D0
- U6 pad 17: /DA -> (no net)
- U6 pad 18: /RDA -> /RaspberryPi/SDX_D1
- U6 pad 19: /CB2 -> GND
- U6 pad 2: /PA0 -> (no net)
- U6 pad 20: +5V -> GND
- U6 pad 21: /RW -> (no net)
- U6 pad 22: /A4 -> /RaspberryPi/SDX_D2
- U6 pad 23: /$D000 -> (no net)
- U6 pad 24: +5V -> /RaspberryPi/SDX_D3
- U6 pad 25: /PHI2O -> GND
- U6 pad 26: /D7 -> GND
- U6 pad 27: /D6 -> (no net)
- U6 pad 28: /D5 -> /RaspberryPi/RP_STB
- U6 pad 29: /D4 -> (no net)
- U6 pad 3: /PA1 -> (no net)
- U6 pad 30: /D3 -> /RaspberryPi/RP_PA0
- U6 pad 31: /D2 -> GND
- U6 pad 32: /D1 -> GND
- U6 pad 33: /D0 -> (no net)
- U6 pad 34: /RESET -> /RaspberryPi/RP_PA1
- U6 pad 35: /A1 -> (no net)
- U6 pad 36: /A0 -> /RaspberryPi/RP_PA2
- U6 pad 37: (no net) -> GND
- U6 pad 38: (no net) -> GND
- U6 pad 39: (no net) -> +3V3
- U6 pad 4: /PA2 -> +3V3
- U6 pad 40: /STROBE -> +3V3
- U6 pad 5: /PA3 -> (no net)
- U6 pad 6: /PA4 -> +3V3
- U6 pad 7: /PA5 -> GND
- U6 pad 8: /PA6 -> GND
- U6 pad 9: +5V -> (no net)
- U8 pad 1: (no net) -> +5V
- U8 pad 10: /A0 -> +1V8
- U8 pad 11: /D0 -> (no net)
- U8 pad 12: /D1 -> Net-(C3-Pad2)
- U8 pad 13: /D2 -> GND
- U8 pad 2: /A12 -> Net-(L2-Pad1)
- U8 pad 3: /A7 -> GND
- U8 pad 4: /A6 -> +3V3
- U8 pad 5: /A5 -> (no net)
- U8 pad 6: /A4 -> +5V
- U8 pad 7: /A3 -> +5V
- U8 pad 8: /A2 -> Net-(L1-Pad1)
- U8 pad 9: /A1 -> GND
- U9 pad 1: GND -> /$E000
- U9 pad 10: /RaspberryPi/SDX_CLK -> /RW
- U9 pad 11: (no net) -> /WE
- U9 pad 12: /RaspberryPi/SDX_CMD -> /PHI2O
- U9 pad 13: GND -> Net-(U9-Pad13)
- U9 pad 14: GND -> +5V
- U9 pad 2: (no net) -> /$F000
- U9 pad 3: Net-(R15-Pad1) -> Net-(U9-Pad3)
- U9 pad 4: +3V3 -> Net-(U9-Pad3)
- U9 pad 5: /RaspberryPi/CLEAR -> Net-(U9-Pad3)
- U9 pad 6: +3V3 -> Net-(U4-Pad20)
- U9 pad 8: GND -> Net-(U9-Pad13)
- U9 pad 9: (no net) -> /RW
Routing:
- net +5V: track 0.00 -> 449.7 mm, vias 0 -> 7
- net /A12: track 0.00 -> 220.2 mm
- net /A11: track 0.00 -> 214.6 mm, vias 0 -> 1
- net GND: track 0.00 -> 214.4 mm, vias 0 -> 1
- net /A6: track 0.00 -> 211.4 mm
- net /A4: track 0.00 -> 210.7 mm, vias 0 -> 1
- net /A9: track 0.00 -> 209.4 mm
- net /A7: track 0.00 -> 206.5 mm
- net /A8: track 0.00 -> 205.7 mm
- net /A5: track 0.00 -> 199.7 mm
- net /D7: track 0.00 -> 197.6 mm, vias 0 -> 1
- net /A14: track 0.00 -> 197.5 mm
- net /A2: track 0.00 -> 192.7 mm
- net /A3: track 0.00 -> 190.6 mm
- net /A1: track 0.00 -> 189.1 mm, vias 0 -> 1
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- added copper zone on B.Cu, net GND
- added copper zone on F.Cu, net GND
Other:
- net class All added: clearance 0.2, trace_width 0.4, via_dia 1.2, via_drill 0.7
- net class Default: clearance 0.2 -> 0.15; trace_width 0.4 -> 0.15; via_dia 0.7 -> 1.2; via_drill 0.4 -> 0.7
- net class HDMI added: clearance 0.15, trace_width 0.15, via_dia 1.2, via_drill 0.7
- net class HDMI_dPair removed
- net class PWR: via_dia 1 -> 1.2; via_drill 0.6 -> 0.7
- net class RPi added: clearance 0.2, trace_width 0.25, via_dia 1.2, via_drill 0.7
- net class USB_dPair: clearance 0.2 -> 0.15; trace_width 0.2 -> 0.3; via_dia 1 -> 1.2; via_drill 0.6 -> 0.7
- rule trace_clearance: 0.2 -> 0.15
